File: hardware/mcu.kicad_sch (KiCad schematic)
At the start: 19 parts, among them J2 Conn_01x03_Socket, J3 Conn_01x03_Socket, SW1 SW_Push, U1 STM32F405RGT7

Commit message: feat(kicad): Added heirarchical nodes for baro, imu. Added motor driving logic and updated pinouts
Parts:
- added C22, C23: 26p, Capacitor_SMD:C_0603_1608Metric, symbol Device:C
- added J4: Conn_01x04_Pin, symbol Connector:Conn_01x04_Pin
- added R10, R11, R8, R9: 2k2, Resistor_SMD:R_0402_1005Metric, symbol Device:R
- added X1: 8MHz, ABM3B_ABR, symbol 2026-10-13_21-16-43:ABM3B-8.000MHZ-B2-T
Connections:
- net +3V3: now also J4.1 (Pin_1), R11.2, R8.1, R9.1
- net GND: now also C22.2, C23.2, J4.4 (Pin_4), X1.2, X1.4
- net I2C1_SCL: now also R8.2
- net I2C1_SDA: now also R9.2
- net I2C2_SCL: now also J4.3 (Pin_3), R10.1
- net I2C2_SDA: now also J4.2 (Pin_2), R11.1
- net HSE_IN: now reaches U1.5 (PH0)
- net HSE_IN: now also C22.1, X1.1
- net HSE_OUT: now reaches U1.6 (PH1)
- net HSE_OUT: now also C23.1, X1.3
- net I2C3_SCL: no longer names the net of U1.41 (PA8)
- net I2C3_SDA: no longer names the net of U1.40 (PC9)
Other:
- moved on the sheet: C10, R1, R2, SW1

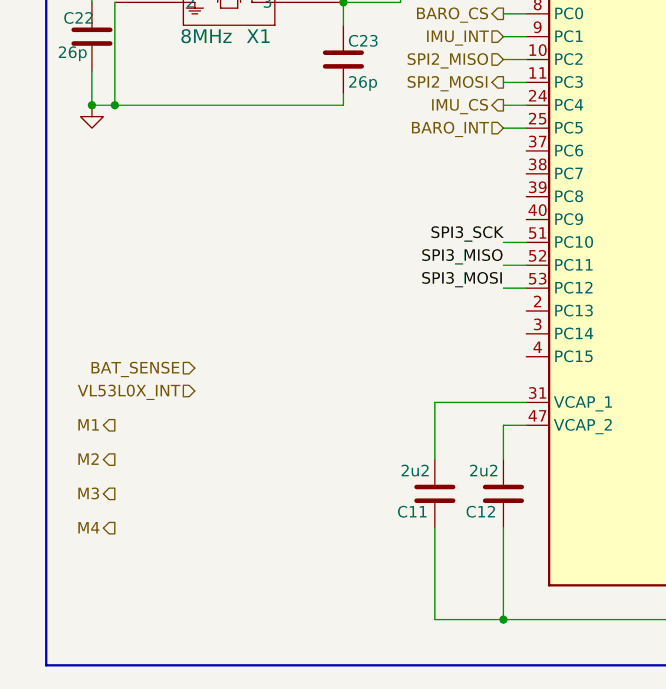
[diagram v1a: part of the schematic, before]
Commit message: feat(kicad): Added several open sourced footprint libraries, finished schematic design for nrf, uwb, tof, flash, motors and added all reference material to refs folder
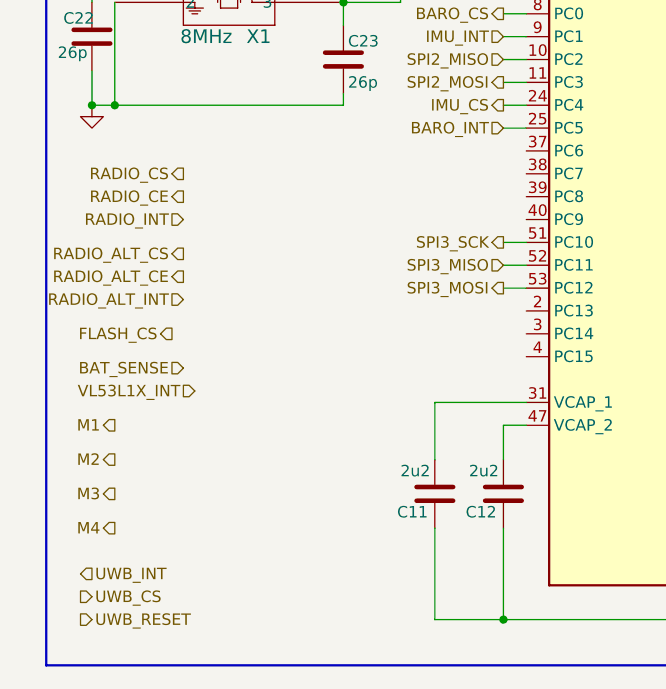
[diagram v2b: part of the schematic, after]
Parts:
- X1: footprint ABM3B_ABR -> (none)
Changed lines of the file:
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@@
 		)
 	)
-	(label "SPI3_MISO"
-		(at 124.46 106.68 180)
-		(effects
-			(font
-				(size 1.27 1.27)
-			)
-			(justify right bottom)
-		)
-	)
 	(label "SWDIO"
 		(at 167.64 88.9 0)
@@
 		)
 	)
-	(label "SPI3_MOSI"
-		(at 124.46 109.22 180)
-		(effects
-			(font
-				(size 1.27 1.27)
-			)
-			(justify right bottom)
-		)
-	)
-	(label "SPI3_SCK"
-		(at 124.46 104.14 180)
-		(effects
-			(font
-				(size 1.27 1.27)
-			)
-			(justify right bottom)
-		)
-	)
 	(label "HSE_OUT"
 		(at 127 68.58 180)
@@
 		)
 	)
+	(hierarchical_label "SPI3_MISO"
+		(shape input)
+		(at 124.46 106.68 180)
+		(effects
+			(font
+				(size 1.27 1.27)
+			)
+			(justify right)
+		)
+	)
+	(hierarchical_label "RADIO_INT"
+		(shape input)
+		(at 88.9 101.6 180)
+		(effects
+			(font
+				(size 1.27 1.27)
+			)
+			(justify right)
+		)
+	)
 	(hierarchical_label "SPI2_MISO"
 		(shape input)
@@
 		)
 	)
+	(hierarchical_label "RADIO_ALT_CE"
+		(shape output)
+		(at 88.9 107.95 180)
+		(effects
+			(font
+				(size 1.27 1.27)
+			)
+			(justify right)
+		)
+	)
 	(hierarchical_label "IMU_CS"
 		(shape output)
@@
 		)
 	)
+	(hierarchical_label "RADIO_ALT_CS"
+		(shape output)
+		(at 88.9 105.41 180)
+		(effects
+			(font
+				(size 1.27 1.27)
+			)
+			(justify right)
+		)
+	)
+	(hierarchical_label "RADIO_ALT_INT"
+		(shape input)
+		(at 88.9 110.49 180)
+		(effects
+			(font
+				(size 1.27 1.27)
+			)
+			(justify right)
+		)
+	)
+	(hierarchical_label "FLASH_CS"
+		(shape output)
+		(at 87.63 114.3 180)
+		(effects
+			(font
+				(size 1.27 1.27)
+			)
+			(justify right)
+		)
+	)
+	(hierarchical_label "UWB_CS"
+		(shape output)
+		(at 77.47 143.51 0)
+		(effects
+			(font
+				(size 1.27 1.27)
+			)
+			(justify left)
+		)
+	)
 	(hierarchical_label "BAT_SENSE"
 		(shape input)
-		(at 90.17 118.11 180)
+		(at 88.9 118.11 180)
+		(effects
+			(font
+				(size 1.27 1.27)
+			)
+			(justify right)
+		)
+	)
+	(hierarchical_label "UWB_INT"
+		(shape input)
+		(at 77.47 140.97 0)
+		(effects
+			(font
+				(size 1.27 1.27)
+			)
+			(justify left)
+		)
+	)
+	(hierarchical_label "SPI3_SCK"
+		(shape output)
+		(at 124.46 104.14 180)
 		(effects
 			(font
@@
 		)
 	)
-	(hierarchical_label "VL53L0X_INT"
+	(hierarchical_label "UWB_RESET"
+		(shape output)
+		(at 77.47 146.05 0)
+		(effects
+			(font
+				(size 1.27 1.27)
+			)
+			(justify left)
+		)
+	)
+	(hierarchical_label "RADIO_CS"
+		(shape output)
+		(at 88.9 96.52 180)
+		(effects
+			(font
+				(size 1.27 1.27)
+			)
+			(justify right)
+		)
+	)
+	(hierarchical_label "VL53L1X_INT"
 		(shape input)
 		(at 90.17 120.65 180)
@@
 		)
 	)
+	(hierarchical_label "RADIO_CE"
+		(shape output)
+		(at 88.9 99.06 180)
+		(effects
+			(font
+				(size 1.27 1.27)
+			)
+			(justify right)
+		)
+	)
 	(hierarchical_label "SPI2_SCK"
 		(shape output)
@@
 		)
 	)
+	(hierarchical_label "SPI3_MOSI"
+		(shape output)
+		(at 124.46 109.22 180)
+		(effects
+			(font
+				(size 1.27 1.27)
+			)
+			(justify right)
+		)
+	)
 	(hierarchical_label "SPI2_MOSI"
 		(shape output)
@@
 			)
 		)
-		(property "Footprint" "ABM3B_ABR"
+		(property "Footprint" ""
 			(at 81.28 74.93 0)
 			(hide yes)

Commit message: feat(kicad): Finished initial draft of the schematic design All pinouts are set
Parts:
- added D10, D5, D6, D7, D8, D9: LED, symbol Device:LED
- added R22, R23, R24, R25, R26, R27: 330R, Resistor_SMD:R_0402_1005Metric, symbol Device:R
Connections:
- net +3V3: now also R10.2
- net BARO_CS: now also U1.9 (PC1); no longer U1.8 (PC0)
- net BARO_INT: now also U1.8 (PC0); no longer U1.25 (PC5)
- net BAT_SENSE: now also U1.15 (PA1)
- net FLASH_CS: now also U1.28 (PB2)
- net GND: now also C23.1, D10.1 (K), D5.1 (K), D6.1 (K), D7.1 (K), D8.1 (K), D9.1 (K); no longer C23.2
- net HSE_OUT: now also C23.2; no longer C23.1
- net I2C1_SCL: now also R9.2, U1.58 (PB6); no longer R8.2, U1.61 (PB8)
- net I2C1_SDA: now also R8.2; no longer R9.2
- net IMU_CS: now also U1.44 (PA11); no longer U1.24 (PC4)
- net IMU_INT: now also U1.45 (PA12); no longer U1.9 (PC1)
- net M1: now also U1.62 (PB9)
- net M2: now also U1.50 (PA15)
- net M3: now also U1.35 (PB14)
- net M4: now also U1.14 (PA0)
- net RADIO_ALT_CE: now also U1.3 (PC14)
- net RADIO_ALT_CS: now also U1.2 (PC13)
- net RADIO_ALT_INT: now also U1.4 (PC15)
- net RADIO_CE: now also U1.56 (PB4)
- net RADIO_CS: now also U1.57 (PB5)
- net RADIO_INT: now also U1.55 (PB3)
- net UWB_CS: now also U1.25 (PC5)
- net UWB_INT: now also U1.24 (PC4)
- net UWB_RESET: now also U1.26 (PB0)
- net VL53L1X_INT: now also U1.33 (PB12)
- net VL53L1X_LED: now reaches U1.36 (PB15)
- net VL53L1X_LED: now also R27.1
- net FLASH_LED: now reaches U1.37 (PC6)
- net FLASH_LED: now also R26.1
- net RADIO_LED: now reaches U1.38 (PC7)
- net RADIO_LED: now also R25.1
- net UWB_LED: now reaches U1.39 (PC8)
- net UWB_LED: now also R24.1
- net BARO_LED: now reaches U1.40 (PC9)
- net BARO_LED: now also R23.1
- net IMU_LED: now reaches U1.41 (PA8)
- net IMU_LED: now also R22.1
- new net: D8.2 (A), R25.2
- new net: D6.2 (A), R23.2
- new net: D9.2 (A), R26.2
- new net: D5.2 (A), R22.2
- new net: D7.2 (A), R24.2
- new net: D10.2 (A), R27.2
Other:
- moved on the sheet: C23, J4, R10, R11, R8, R9

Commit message: feat(kicad): Cleared ERC errors and assigned footprints for all parts
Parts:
- removed J4: Conn_01x04_Pin, symbol Connector:Conn_01x04_Pin
- added TP1: GND, TestPoint:TestPoint_Pad_D1.5mm, symbol Connector:TestPoint
- added TP2: I2C2_SCL, TestPoint:TestPoint_Pad_D1.5mm, symbol Connector:TestPoint
- added TP3: I2C2_SDA, TestPoint:TestPoint_Pad_D1.5mm, symbol Connector:TestPoint
- added TP4: +3V3, TestPoint:TestPoint_Pad_D1.5mm, symbol Connector:TestPoint
- C22, C23: footprint Capacitor_SMD:C_0603_1608Metric -> Capacitor_SMD:C_0402_1005Metric
- D10, D5, D6, D7, D8, D9: footprint (none) -> LED_SMD:LED_0603_1608Metric
- X1: footprint (none) -> abm:ABM3B_ABR
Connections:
- net +3V3: now also TP4.1
- net GND: now also TP1.1
- net I2C2_SCL: now also TP2.1
- net I2C2_SDA: now also TP3.1
- no-connect marks 0 -> 6

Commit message: feat(kicad): Added mcu application notes
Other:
- note added: "Application Notes 1)SPI lines should be as short as possible 2)Decoupling caps should be really close to the power pins 3)Crystal should be very close to the MCU PINS"
- moved on the sheet: C1, C10, C11, C12, C2, C22, C23, C3, C4, C5, C6, C7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

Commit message: feat(kicad): Added step files for missing parts
changed flyback diode to SMA part with 5A max

Redid initial layout
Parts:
- removed R10, R11: 2k2, Resistor_SMD:R_0402_1005Metric, symbol Device:R
- removed TP1: GND, TestPoint:TestPoint_Pad_D1.5mm, symbol Connector:TestPoint
- removed TP2: I2C2_SCL, TestPoint:TestPoint_Pad_D1.5mm, symbol Connector:TestPoint
- removed TP3: I2C2_SDA, TestPoint:TestPoint_Pad_D1.5mm, symbol Connector:TestPoint
- removed TP4: +3V3, TestPoint:TestPoint_Pad_D1.5mm, symbol Connector:TestPoint
- SW1: footprint Button_Switch_SMD:SW_Push_1P1T_NO_CK_KSC6xxG -> Button_Switch_SMD:SW_SPST_TS-1088-xR020
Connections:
- net I2C2_SCL: no longer names the net of U1.29 (PB10)
- net I2C2_SDA: no longer names the net of U1.30 (PB11)
- no-connect marks 6 -> 8

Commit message: feat(kicad): Updated schematic to keep traces shorter on the layout Restarting layout
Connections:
- net BARO_CS: now also U1.44 (PA11); no longer U1.9 (PC1)
- net BARO_INT: now also U1.45 (PA12); no longer U1.8 (PC0)
- net IMU_CS: now also U1.17 (PA3); no longer U1.44 (PA11)
- net IMU_INT: now also U1.20 (PA4); no longer U1.45 (PA12)
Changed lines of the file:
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@@
-	)
-	(no_connect
-		(at 167.64 58.42)
 	)
 	(no_connect
@@
 	)
 	(no_connect
+		(at 127 73.66)
+	)
+	(no_connect
+		(at 127 71.12)
+	)
+	(no_connect
 		(at 167.64 119.38)
-	)
-	(no_connect
-		(at 167.64 55.88)
 	)
 	(no_connect
@@
 	(wire
 		(pts
-			(xy 123.19 71.12) (xy 127 71.12)
-		)
-		(stroke
-			(width 0)
-			(type default)
-		)
-	)
-	(wire
-		(pts
 			(xy 81.28 69.85) (xy 81.28 81.28)
 		)
@@
 		(pts
 			(xy 167.64 114.3) (xy 168.91 114.3)
-		)
-		(stroke
-			(width 0)
-			(type default)
-		)
-	)
-	(wire
-		(pts
-			(xy 123.19 73.66) (xy 127 73.66)
 		)
 		(stroke
@@
 	(hierarchical_label "BARO_CS"
 		(shape output)
-		(at 123.19 73.66 180)
-		(effects
-			(font
-				(size 1.27 1.27)
-			)
-			(justify right)
+		(at 167.64 76.2 0)
+		(effects
+			(font
+				(size 1.27 1.27)
+			)
+			(justify left)
 		)
 	)
@@
 	(hierarchical_label "IMU_CS"
 		(shape output)
-		(at 167.64 76.2 0)
+		(at 167.64 55.88 0)
 		(effects
 			(font
@@
 		)
 	)
+	(hierarchical_label "IMU_INT"
+		(shape input)
+		(at 167.64 58.42 0)
+		(effects
+			(font
+				(size 1.27 1.27)
+			)
+			(justify left)
+		)
+	)
 	(hierarchical_label "UWB_CS"
 		(shape output)
@@
 		)
 	)
-	(hierarchical_label "IMU_INT"
+	(hierarchical_label "BARO_INT"
 		(shape input)
 		(at 167.64 78.74 0)
@@
 		)
 	)
-	(hierarchical_label "BARO_INT"
-		(shape input)
-		(at 123.19 71.12 180)
-		(effects
-			(font
-				(size 1.27 1.27)
-			)
-			(justify right)
-		)
-	)
